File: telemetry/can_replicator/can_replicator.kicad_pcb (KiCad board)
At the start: 2 copper layers, 33 parts, among them J1 CONN_02X03, J2 MM_M_VT_20, U1 MCP2561-E_SN, U2 ATMEGA16M1, U3 USB_MicroB, U4 FT232RL, Y1 Crystal_SMD

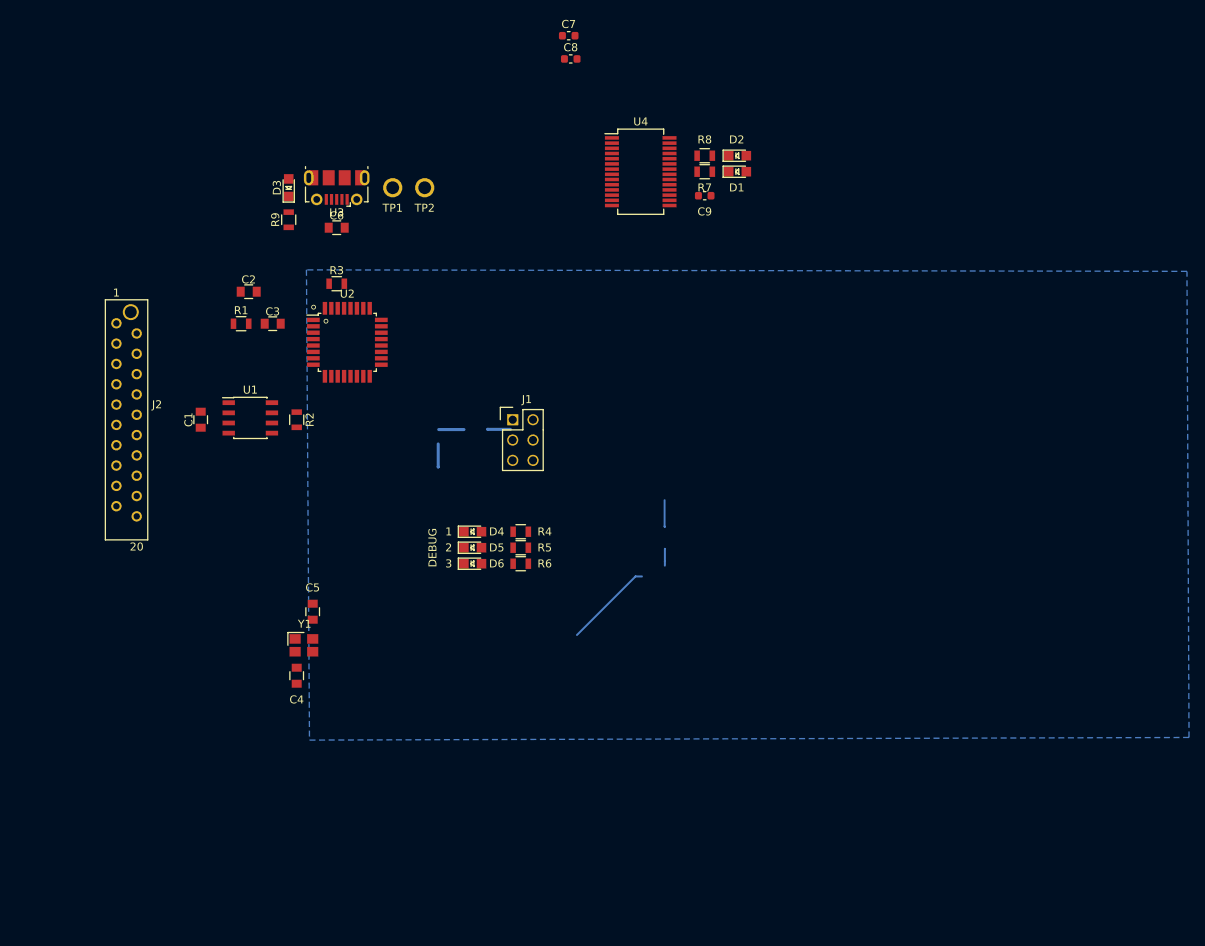
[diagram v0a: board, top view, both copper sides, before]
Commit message: fix: begin removal of template-rescue
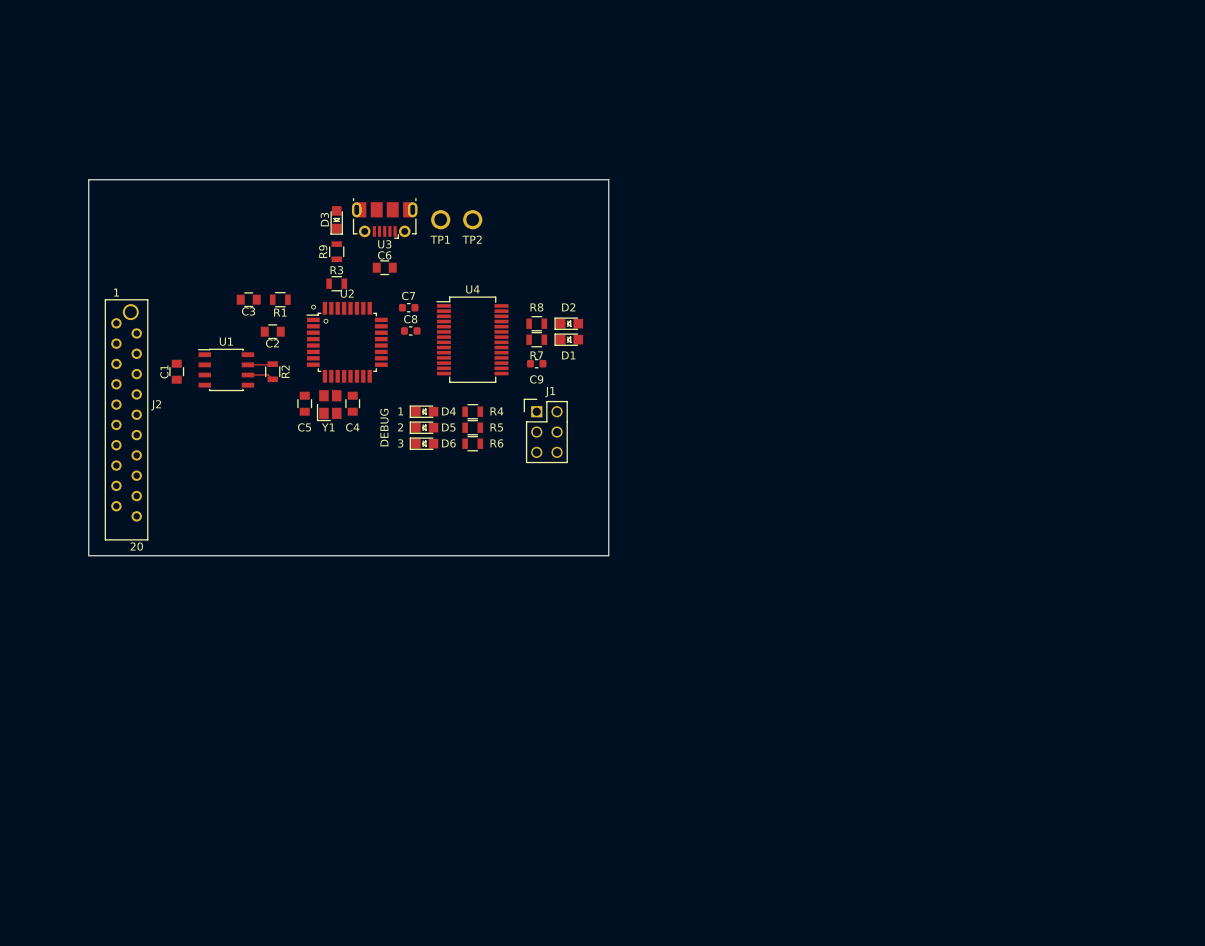
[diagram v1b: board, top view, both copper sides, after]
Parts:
- moved C7 39.4 mm to (111.0, 81.0)
- moved C8 39.4 mm to (111.3, 83.9)
- moved C4 34.7 mm to (104.0, 93.0), turned to 90 degrees
- moved Y1 30.3 mm to (101.2, 93.1), turned to 90 degrees
- moved C9 29.7 mm to (127.0, 88.0)
- moved D1 29.7 mm to (131.1, 85.0)
- moved D2 29.7 mm to (131.1, 83.0)
- moved R7 29.7 mm to (127.0, 85.0)
- moved R8 29.7 mm to (127.0, 83.0)
- moved U4 29.7 mm to (119.0, 85.0)
- moved C5 26.0 mm to (98.0, 93.0), turned to 270 degrees
- moved D4 16.2 mm to (113.0, 94.0)
- moved D5 16.2 mm to (113.0, 96.0)
- moved D6 16.2 mm to (113.0, 98.0)
- moved R4 16.2 mm to (119.0, 94.0)
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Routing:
- net GND: track 25.5 -> 0.00 mm
- net /CAN_-: track 0.00 -> 3.32 mm
- net /CAN_+: track 0.00 -> 3.13 mm
- removed copper zone on B.Cu, net GND
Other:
- board outline added: 65 x 47 mm

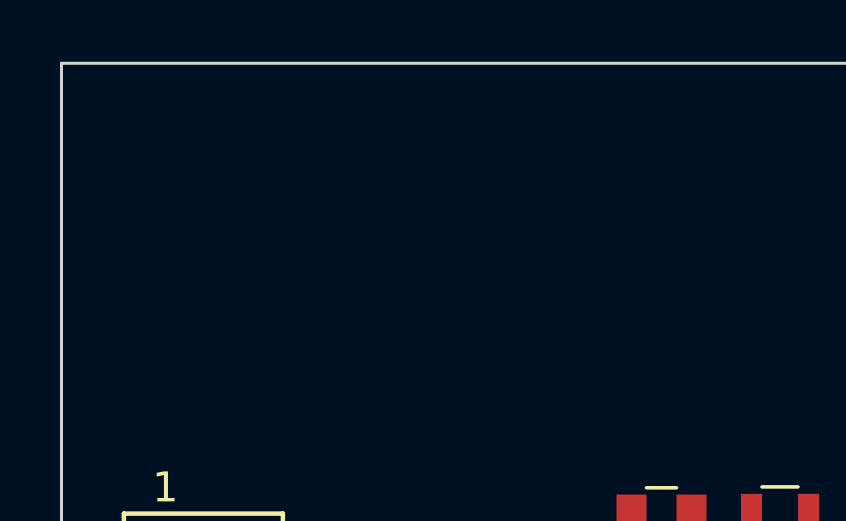
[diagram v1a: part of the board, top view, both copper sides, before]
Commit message: fix: cleanup schematic based on DR feedback
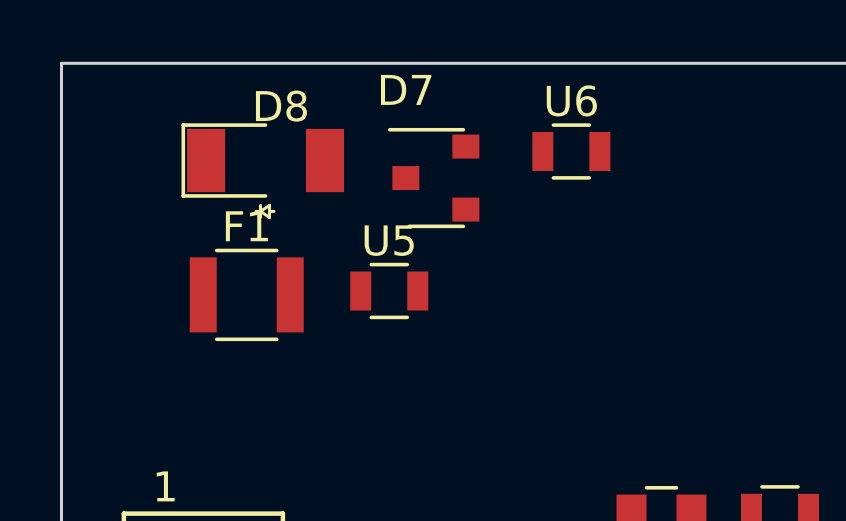
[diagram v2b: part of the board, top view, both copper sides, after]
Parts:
- added D7: BAT400D-7-F, footprints:SOT-23-3_OEM, F.Cu at (82.5, 68.8)
- added D8: D_Zener_5.6V, footprints:D_5.6V_Zener, F.Cu at (77.8, 68.2)
- added F1: F_500mA_16V, footprints:Fuse_1210, F.Cu at (77.2, 72.7)
- added U5: R_500, footprints:R_0805_OEM, F.Cu at (81.9, 72.6)
- added U6: R_500, footprints:R_0805_OEM, F.Cu at (88.0, 67.9)
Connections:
- C1 pad 1: VCC -> +5V
- C2 pad 1: VCC -> +5V
- C6 pad 2: VCC -> +5V
- C7 pad 1: VCC -> +5V
- C8 pad 1: VCC -> +5V
- D1 pad 2: VCC -> +5V
- D2 pad 2: VCC -> +5V
- D3 pad 2: VCC -> +5V
- J1 pad 2: VCC -> +5V
- R1 pad 1: VCC -> +5V
- R3 pad 1: VCC -> +5V
- TP2 pad 1: VCC -> Net-(F1-Pad2)
- U1 pad 3: VCC -> +5V
- U2 pad 1: Net-(U2-Pad1) -> /MISO
- U2 pad 12: /USB_RXD -> /SCK
- U2 pad 2: /USB_TXD -> /MOSI
- U2 pad 28: /SCK -> Net-(U2-Pad28)
- U2 pad 4: VCC -> +5V
- U2 pad 8: /MISO -> Net-(U2-Pad8)
- U2 pad 9: /MOSI -> Net-(U2-Pad9)
- U3 pad 1: VCC -> Net-(F1-Pad2)
- U4 pad 19: VCC -> +5V
- U4 pad 20: VCC -> +5V
- U4 pad 4: VCC -> +5V

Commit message: feat: USB and power
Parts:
- added J3: CONN_01x02, Connector_PinHeader_2.54mm:PinHeader_1x02_P2.54mm_Vertical, F.Cu at (73.7, 107.0)
- added J4: CONN_01x02, Connector_PinHeader_2.54mm:PinHeader_1x02_P2.54mm_Vertical, F.Cu at (86.4, 106.7)
- added R12: R_120, footprints:R_0805_OEM, F.Cu at (82.2, 106.1)
- added R2: R_120, footprints:R_0805_OEM, F.Cu at (77.5, 106.7)
- J2: footprint footprints:micromatch_female_vert_20 -> footprints:micromatch_female_ra_20
- moved Y1 66.5 mm to (132.9, 151.5)
- moved U2 66.5 mm to (135.1, 143.7)
- moved C1 66.5 mm to (113.8, 147.4)
- moved C2 66.5 mm to (125.8, 142.4)
- moved C3 66.5 mm to (122.8, 138.4)
- moved C4 66.5 mm to (135.8, 151.4)
- moved C5 66.5 mm to (129.8, 151.4)
- moved C7 66.5 mm to (142.8, 139.4)
- moved C8 66.5 mm to (143.0, 142.3)
- moved J1 66.5 mm to (158.8, 152.4)
- moved R1 66.5 mm to (126.7, 138.4)
- moved R2 66.5 mm to (125.8, 147.4)
- moved R3 66.5 mm to (133.8, 136.4)
- moved U1 66.5 mm to (120.0, 147.2)
- moved J2 42.7 mm to (117.1, 85.0)
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- renumbered U5 to R10, U6 to R11
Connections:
- net /USB_RXD renamed /UART_RXD
- net /USB_TXD renamed /UART_TXD
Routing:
- net +5V: track 0.00 -> 56.3 mm, vias 0 -> 4
- net GND: track 0.00 -> 27.4 mm, vias 0 -> 5
- net /USBD-: track 0.00 -> 21.9 mm
- net /USBD+: track 0.00 -> 20.9 mm
- net Net-(F1-Pad2): track 0.00 -> 11.9 mm
- net /TXLED: track 0.00 -> 9.33 mm
- net Net-(D1-Pad1): track 0.00 -> 3.93 mm
- net Net-(D2-Pad1): track 0.00 -> 3.90 mm
- net Net-(C9-Pad1): track 0.00 -> 3.35 mm
- net /CAN_-: track 3.32 -> 0.00 mm
- net /CAN_+: track 3.13 -> 0.00 mm
- net Net-(D3-Pad1): track 0.00 -> 2.30 mm
- net Net-(D7-Pad2): track 0.00 -> 2.29 mm
- net Net-(U3-Pad6): track 0.00 -> 0.57 mm
- added copper zone on B.Cu, net GND
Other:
- net class USB added: clearance 0.1524, trace_width 0.1524, via_dia 0.6096, via_drill 0.3048

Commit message: feat: layout including all components
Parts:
- removed the R2 at (125.8, 147.4)
- removed TP1, TP2: TP, footprints:tp_1.6mm
- added 5V: Test_Point_SMD, footprints:Test_Point_SMD, F.Cu at (114.0, 67.8)
- added GND: Test_Point_SMD, footprints:Test_Point_SMD, F.Cu at (101.9, 67.7)
- moved J1 76.4 mm to (105.4, 97.8), turned to 90 degrees
- moved C7 63.9 mm to (114.9, 81.9), turned to 90 degrees
- moved C8 63.7 mm to (114.9, 85.1), turned to 270 degrees
- moved Y1 49.5 mm to (101.8, 113.0)
- moved C5 48.6 mm to (98.1, 114.6), turned to 180 degrees
- moved C4 47.0 mm to (105.3, 115.6), turned to 0 degrees
- moved U1 45.7 mm to (97.5, 107.4), turned to 90 degrees
- moved C2 45.3 mm to (103.5, 103.0), turned to 225 degrees
- moved U2 44.9 mm to (108.0, 108.0), turned to 315 degrees
- moved R3 42.1 mm to (110.4, 101.4), turned to 315 degrees
- moved C1 38.4 mm to (98.1, 112.4), turned to 180 degrees
- moved R11 37.2 mm to (114.7, 93.8), turned to 90 degrees
- moved R10 36.5 mm to (113.9, 90.2), turned to 90 degrees
- moved R1 28.0 mm to (110.4, 115.6), turned to 0 degrees
- moved C3 26.3 mm to (113.5, 113.7), turned to 90 degrees
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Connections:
- U2 pad 16: /DBG1 -> Net-(U2-Pad16)
- U2 pad 22: Net-(U2-Pad22) -> /DBG1
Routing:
- net +5V: track 56.3 -> 158.9 mm, vias 4 -> 0
- net /RXLED: track 0.00 -> 88.9 mm
- net /TXLED: track 9.33 -> 87.8 mm
- net /SCK: track 0.00 -> 31.4 mm
- net /CAN_+: track 0.00 -> 24.7 mm
- net /MOSI: track 0.00 -> 22.2 mm
- net GND: track 27.4 -> 48.9 mm, vias 5 -> 18
- net /CAN_-: track 0.00 -> 17.8 mm
- net Net-(U3-Pad6): track 0.57 -> 12.4 mm
- net /CAN_TX: track 0.00 -> 11.2 mm
- net /DBG1: track 0.00 -> 9.52 mm
- net Net-(C4-Pad1): track 0.00 -> 7.90 mm
- net /DBG2: track 0.00 -> 6.95 mm
- net Net-(C5-Pad1): track 0.00 -> 6.94 mm
- net Net-(C3-Pad1): track 0.00 -> 6.89 mm
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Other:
- board size 65 x 47 mm -> 28.2 x 52.7 mm
- board text added: "PWR"
- board text added: "RX"
- board text added: "TX"
- board text added: "USB"

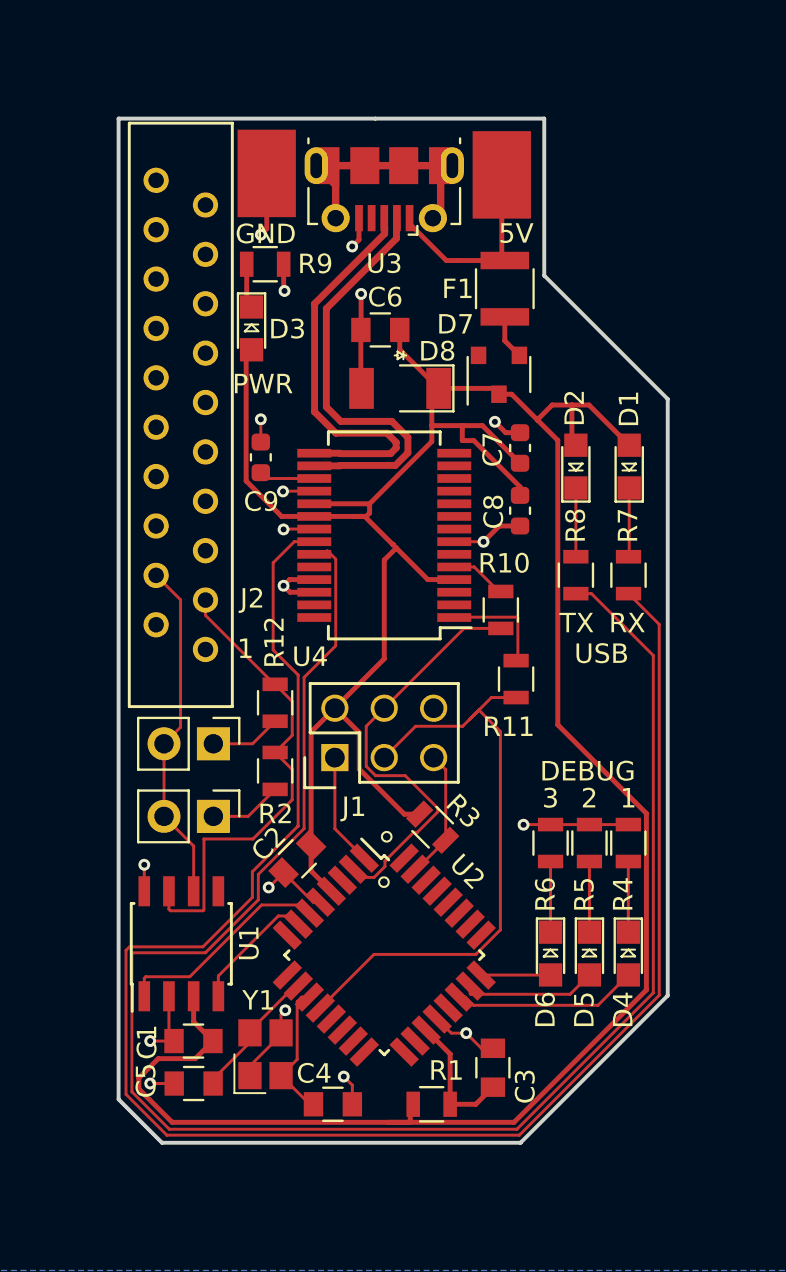
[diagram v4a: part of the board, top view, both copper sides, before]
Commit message: fix: improve routing of USB LEDs
fix: swap to 3 pin headers

fix: improve CAN pair routing

feat: add board info to silkscreen
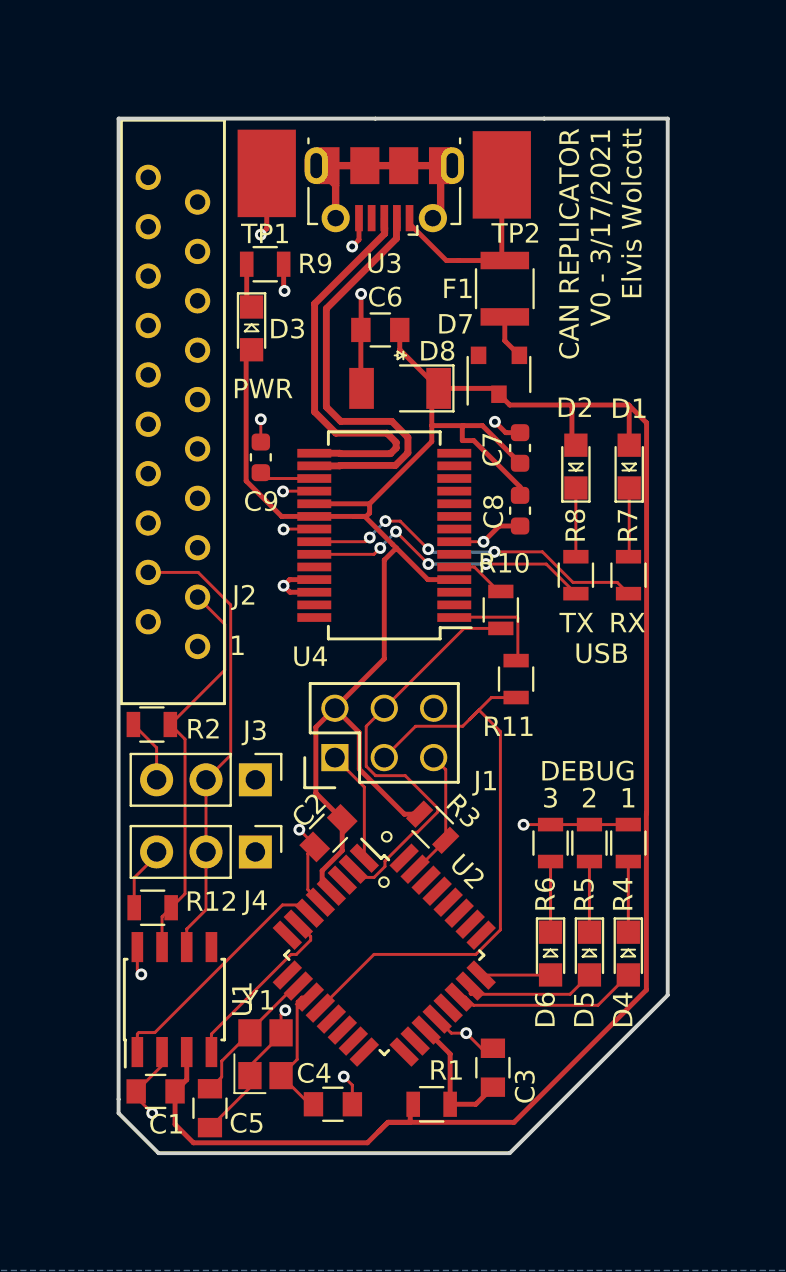
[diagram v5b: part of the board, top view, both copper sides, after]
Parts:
- J3, J4: value CONN_01x02 -> CONN_01X03; footprint Connector_PinHeader_2.54mm:PinHeader_1x02_P2.54mm_Vertical -> Connector_PinHeader_2.54mm:PinHeader_1x03_P2.54mm_Vertical
- moved R12 12.3 mm to (96.0, 105.5), turned to 180 degrees
- moved R2 6.77 mm to (96.0, 96.1), turned to 180 degrees
- moved J4 5.97 mm to (101.3, 102.6)
- moved C1 3.24 mm to (96.2, 115.0)
- moved U1 2.89 mm to (97.2, 110.2)
- moved J3 2.86 mm to (101.3, 98.9)
- moved C2 2.07 mm to (105.1, 101.7)
- moved C5 1.52 mm to (99.0, 115.8), turned to 270 degrees
- moved J2 0.43 mm to (98.3, 87.0)
- renumbered GND to TP1, 5V to TP2
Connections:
- R12 pad 2: Net-(J4-Pad1) -> Net-(J4-Pad3)
- R2 pad 2: Net-(J3-Pad1) -> Net-(J3-Pad3)
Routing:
- net /TXLED: track 87.8 -> 15.3 mm, vias 0 -> 4
- net /RXLED: track 88.9 -> 18.2 mm, vias 0 -> 4
- net /CAN_-: track 17.8 -> 23.5 mm
- net +5V: track 158.9 -> 153.8 mm
- net /CAN_+: track 24.7 -> 20.5 mm
- net Net-(J3-Pad1): track 3.75 -> 0.00 mm
- net Net-(J4-Pad1): track 3.65 -> 0.00 mm
- net GND: track 48.9 -> 52.4 mm, vias 18 -> 17
- net Net-(J4-Pad3): track 0.00 -> 3.35 mm
- net Net-(J3-Pad3): track 0.00 -> 3.34 mm
- net /CAN_RX: track 6.61 -> 9.12 mm
- net /CAN_TX: track 11.2 -> 12.7 mm
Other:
- board size 28.2 x 52.7 mm -> 28.2 x 53.2 mm
- board text added: "CAN REPLICATOR V0 - 3/17/2021 Elvis Wolcott"

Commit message: feat: add OEM logo to back of board
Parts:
- added G***: LOGO, footprints:Logo_Large, B.Cu at (116.6, 87.9)
